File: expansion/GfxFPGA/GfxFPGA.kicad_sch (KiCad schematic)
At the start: 10 parts, among them J101 D68K_64PIN_BOARD, U101 SN74LS125ADR, U102 LD1117S12TR_SOT223

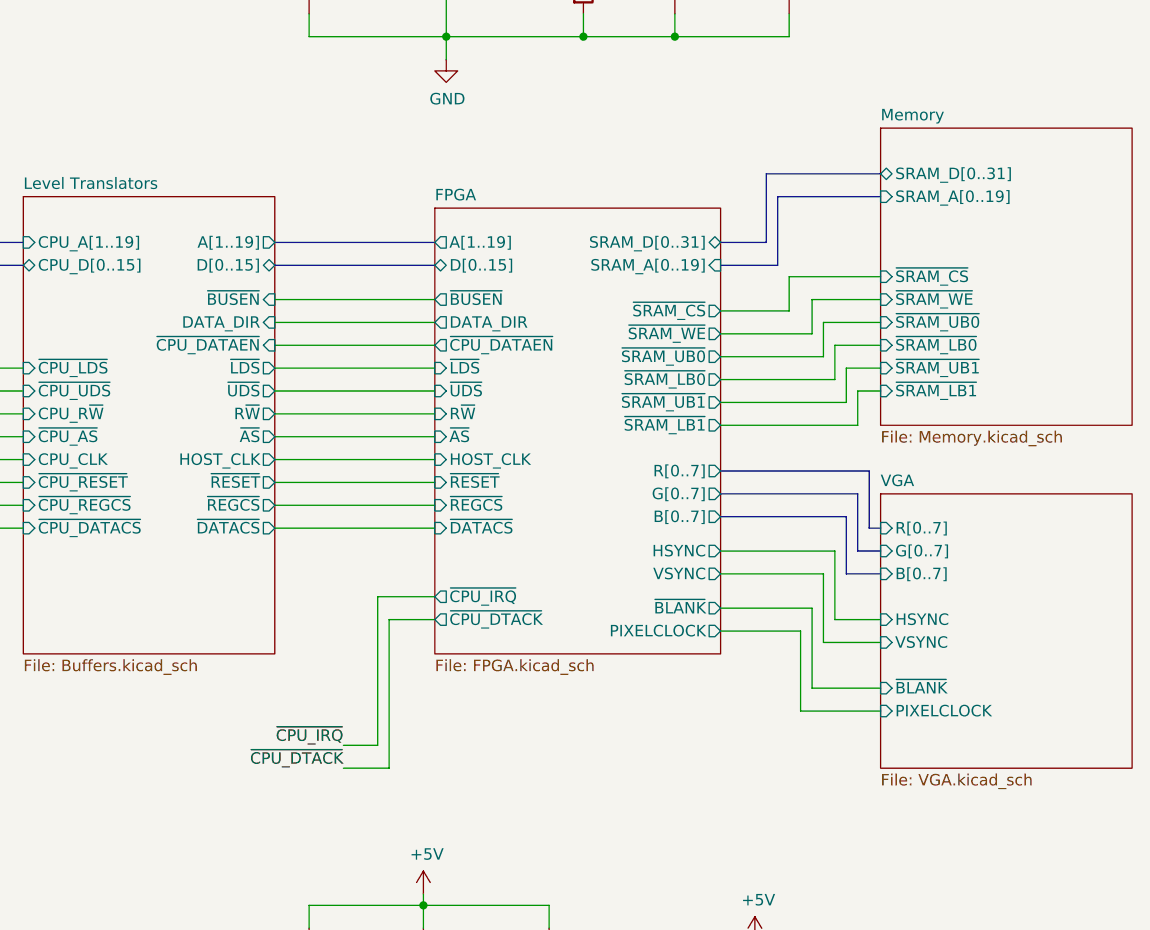
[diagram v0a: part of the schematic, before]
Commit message: WOrking on FPGA VGA board
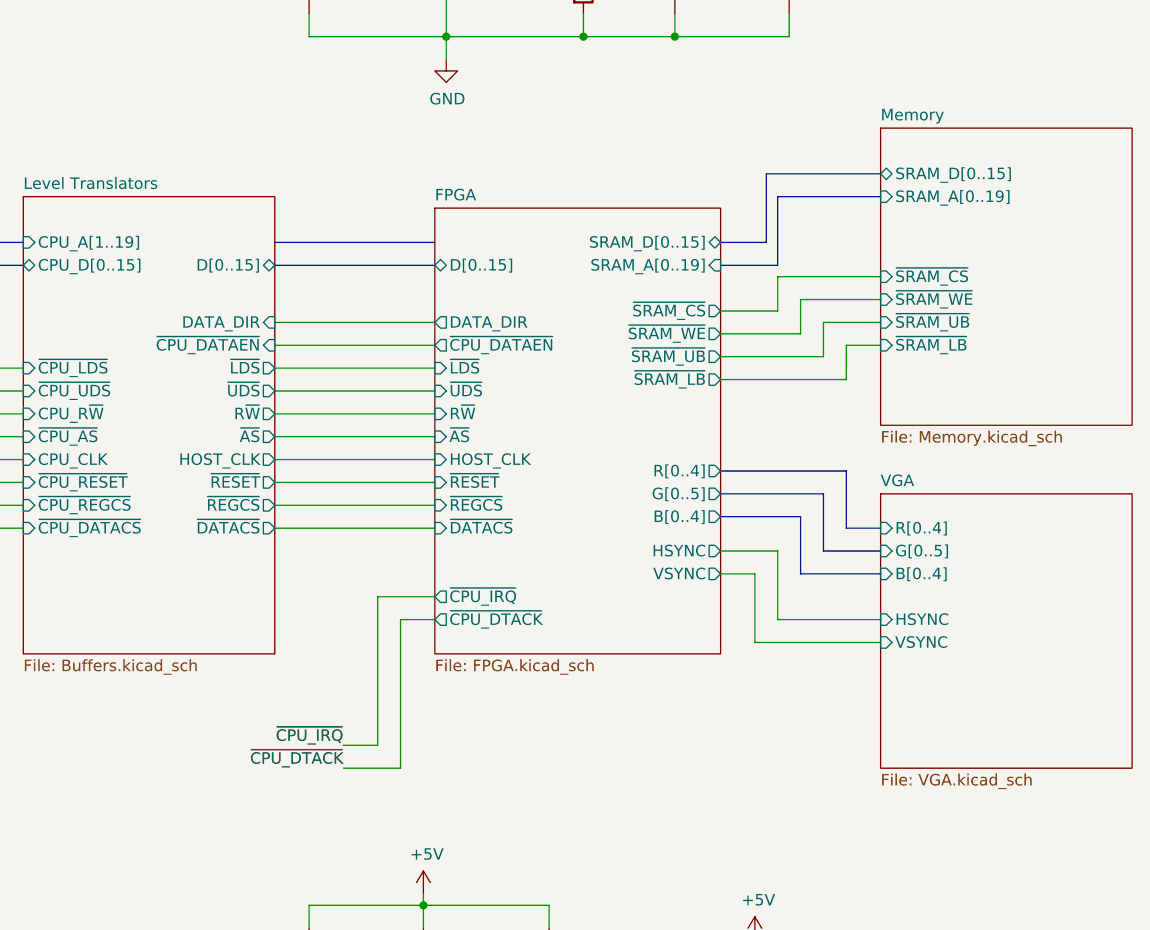
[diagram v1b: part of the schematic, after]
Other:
- sheet FPGA ports: added B[0..4], G[0..5], R[0..4], SRAM_D[0..15], ~{SRAM_LB}, ~{SRAM_UB}; removed A[1..19], B[0..7], G[0..7], PIXELCLOCK, R[0..7], SRAM_D[0..31], ~{BLANK}, ~{BUSEN}, ~{SRAM_LB0}, ~{SRAM_LB1}, ~{SRAM_UB0}, ~{SRAM_UB1}
- sheet Level Translators ports: added none; removed A[1..19], ~{BUSEN}
- sheet Memory ports: added SRAM_D[0..15], ~{SRAM_LB}, ~{SRAM_UB}; removed SRAM_D[0..31], ~{SRAM_LB0}, ~{SRAM_LB1}, ~{SRAM_UB0}, ~{SRAM_UB1}
- sheet VGA ports: added B[0..4], G[0..5], R[0..4]; removed B[0..7], G[0..7], PIXELCLOCK, R[0..7], ~{BLANK}

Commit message: WOrking on VGA card
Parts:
- removed C102: 100nF, Capacitor_SMD:C_0805_2012Metric, symbol Device:C
- added C1, C3, C5: 47uF, Capacitor_SMD:CP_Elec_4x5.3, symbol Device:C_Polarized
- added C4: 100nF, Capacitor_SMD:C_0805_2012Metric, symbol Device:C
- added D1, D2: LED, LED_SMD:LED_1206_3216Metric, symbol Device:LED
- added Q1: BC847, Package_TO_SOT_SMD:SOT-23, symbol Transistor_BJT:BC847
- added R1, R2, R3: 390R, Resistor_SMD:R_0805_2012Metric, symbol Device:R
- added Z1: ~, Ddraig:Ddraig68k-26mm, symbol Ddraig:DdraigLogo
- renumbered C101 to C2, C105 to C6, C103 to C7, C106 to C8, C104 to C9, J101 to J1, R101 to R4, U101 to U1, U102 to U2
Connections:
- net +1V2: now also R1.1
- net +3V3: now also C1.1, C3.1, C4.1, D1.2 (A), R3.1
- net +5V: now also C5.1
- net GND: now also C1.2, C3.2, C4.2, C5.2, D2.1 (K), Q1.2 (E)
- net CPU_CLK: no longer names the net of J1.C23 (SYS_CLK)
- new net: Q1.1 (B), R1.2
- new net: D1.1 (K), R2.1
- new net: Q1.3 (C), R2.2
- new net: D2.2 (A), R3.2
- no-connect marks 10 -> 11
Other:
- sheet FPGA ports: added ADDR_MUX, A[0..9], ~{SRAM_OE}; removed HOST_CLK
- sheet Level Translators ports: added ADDR_MUX, A[0..9]; removed CPU_CLK, HOST_CLK
- sheet Memory ports: added ~{SRAM_OE}; removed none
- moved on the sheet: C7, C9, U1E

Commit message: Updated Audio socket on V9990 board
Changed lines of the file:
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@@
 		(on_board yes)
 		(dnp no)
-		(fields_autoplaced yes)
 		(property "Reference" "Z1"
-			(at 284.48 177.1649 0)
+			(at 277.876 174.244 0)
 			(effects
 				(font
